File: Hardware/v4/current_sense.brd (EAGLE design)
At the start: 69.8 x 59.9 mm, 40 parts, among them J1 SCREW-TERMINAL_2_0.100, J2 SCREW-TERMINAL_2_0.100, J3 SCREW-TERMINAL_2_0.100, J4 SCREW-TERMINAL_2_0.100, U1 MAX9923H, U2 LP3985

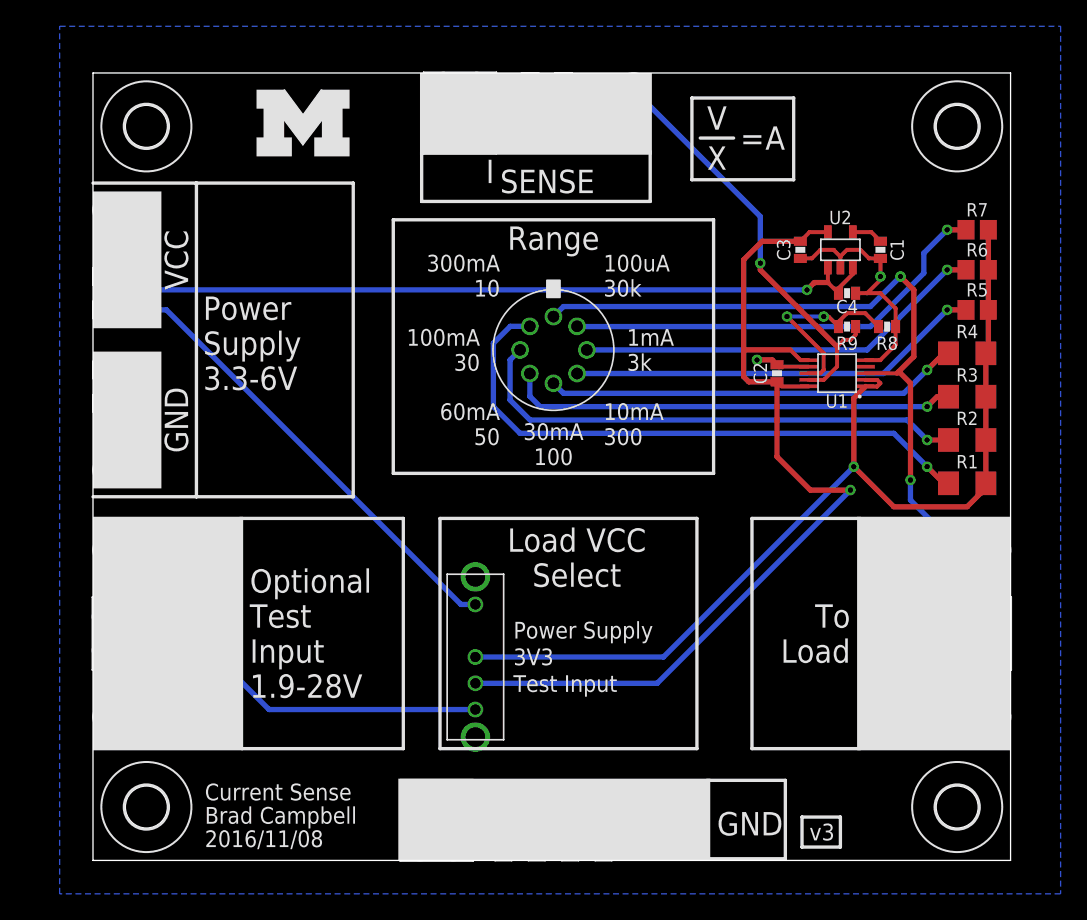
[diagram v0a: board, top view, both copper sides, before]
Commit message: Fix resistance issues, all doc on silk now
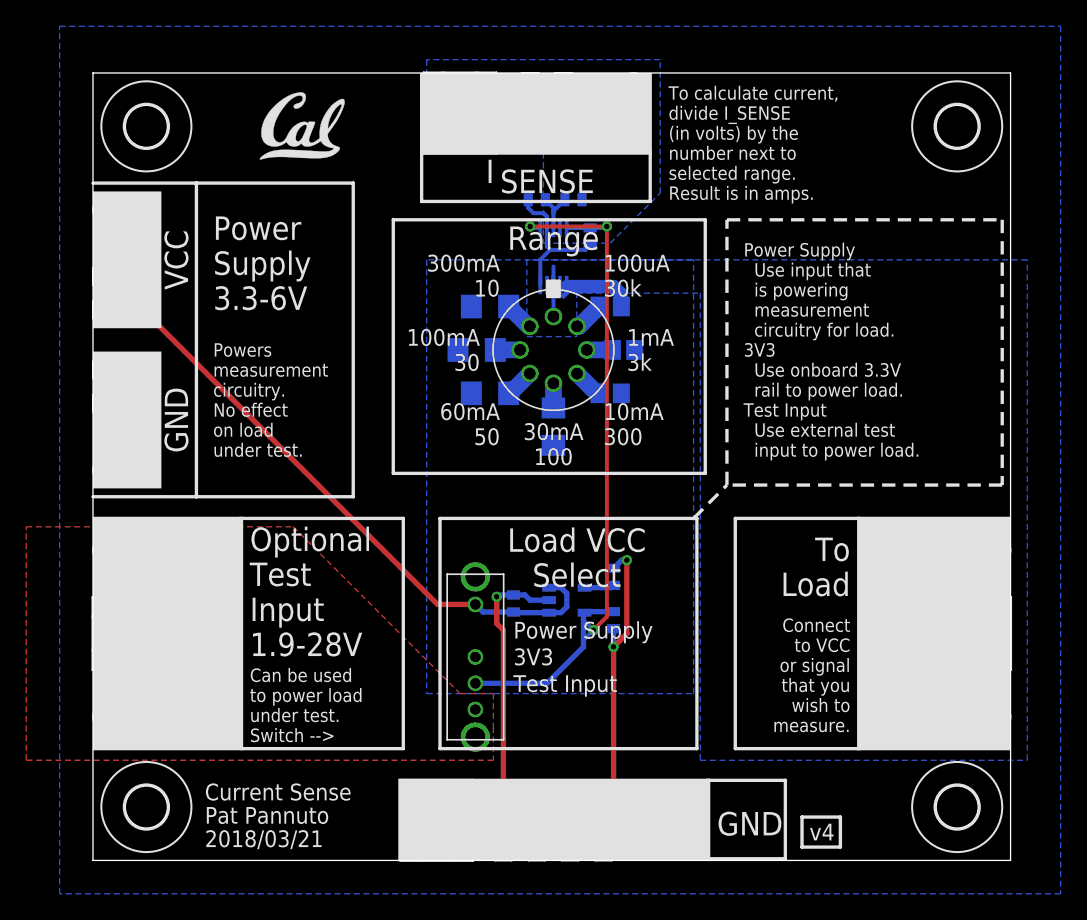
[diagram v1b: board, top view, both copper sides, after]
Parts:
- removed LOGO2: UMICH_SOLID_MEDIUM, logos:UMICH_SOLID_200MIL
- added U$1: (no value), logos:UCB_CAL_200MIL
- moved R1 38.7 mm to (30.2, 42.2), flipped to the bottom
- moved R2 38.0 mm to (29.2, 38.9), flipped to the bottom
- moved R3 36.3 mm to (30.2, 35.6), flipped to the bottom
- moved C4 34.7 mm to (32.0, 19.6), flipped to the bottom, turned to 90 degrees
- moved U2 33.8 mm to (36.1, 19.8), flipped to the bottom, turned to 90 degrees
- moved C1 32.1 mm to (39.6, 21.6), flipped to the bottom, turned to 90 degrees
- moved R4 32.0 mm to (35.1, 33.0), flipped to the bottom, turned to 270 degrees
- moved C3 31.6 mm to (39.6, 18.3), flipped to the bottom
- moved R5 28.7 mm to (39.4, 35.6), flipped to the bottom, turned to 180 degrees
- moved R7 28.5 mm to (39.4, 42.2), flipped to the bottom, turned to 180 degrees
- moved R8 28.4 mm to (33.8, 50.3), flipped to the bottom
- moved R6 27.6 mm to (40.4, 38.9), flipped to the bottom, turned to 180 degrees
- moved U1 23.3 mm to (35.1, 46.0), flipped to the bottom, turned to 0 degrees
- moved R9 23.0 mm to (36.6, 50.3), flipped to the bottom, turned to 180 degrees
- moved C2 17.6 mm to (37.8, 47.5), flipped to the bottom, turned to 270 degrees
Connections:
- net N$1 renamed RS-_100UA
- net N$2 renamed RS-_1MA
- net N$3 renamed RS-_10MA
- net N$4 renamed RS-_30MA
- net N$5 renamed RS-_60MA
- net N$6 renamed RS-_100MA
- net N$7 renamed SENSE_FB
- net N$8 renamed LDO_BYPASS
- net N$9 renamed RS-_300MA
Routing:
- net RS-: track 85.4 -> 3.81 mm, vias 2 -> 0
- net VIN: track 75.4 -> 7.31 mm, vias 1 -> 0
- net VOUT: track 52.4 -> 0.00 mm, vias 1 -> 0
- net LOAD_IN: track 50.5 -> 0.00 mm
- net POWER_SUPPLY: track 104.8 -> 59.8 mm, vias 1 -> 0
- net RS-_300MA: track 45.2 -> 2.23 mm, vias 1 -> 0
- net RS-_100MA: track 38.8 -> 1.88 mm, vias 1 -> 0
- net RS-_60MA: track 34.3 -> 2.23 mm, vias 1 -> 0
- net RS-_100UA: track 33.6 -> 2.30 mm, vias 1 -> 0
- net RS-_30MA: track 31.7 -> 1.88 mm, vias 1 -> 0
- net RS-_1MA: track 31.4 -> 1.94 mm, vias 1 -> 0
- net RS-_10MA: track 31.6 -> 2.30 mm, vias 1 -> 0
- net GND: track 37.1 -> 54.2 mm, vias 2 -> 3
- net VCC: track 73.7 -> 57.3 mm, vias 1 -> 3
- net SENSE_FB: track 14.8 -> 3.64 mm, vias 2 -> 0
- added copper zone on layer 1, net LOAD_IN
- added copper zone on layer 16, net RS-
- added copper zone on layer 16, net VIN
- added copper zone on layer 16, net VOUT
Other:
- board text added: "2018/03/21"
- board text added: "Can be used to power load under test. Switch -->"
- board text added: "Connect to VCC or signal that you wish to measure."
- board text added: "Pat Pannuto"
- board text added: "Power Supply Use input that is powering measurement circuitry for load. 3V3 Use onboard 3.3V rail to power load. Test Input Use external test input to power load."
- board text added: "Powers measurement circuitry. No effect on load under test."
- board text added: "To calculate current, divide I_SENSE (in volts) by the number next to selected range. Result is in amps."
- board text added: "v4"
- board text removed: "2016/11/08"
- board text removed: "="
- board text removed: "A"
- board text removed: "Brad Campbell"
- board text removed: "V"
- board text removed: "X"
- board text removed: "v3"

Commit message: v4: fatten more traces because why not
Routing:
- net GND: track 54.2 -> 56.3 mm, vias 3 -> 5
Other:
- board text added: "2018/03/22"
- board text removed: "2018/03/21"
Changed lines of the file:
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@@
 <setting verticaltext="up"/>
 </settings>
-<grid distance="25" unitdist="mil" unit="mil" style="lines" multiple="1" display="yes" altdistance="10" altunitdist="mil" altunit="mil"/>
+<grid distance="10" unitdist="mil" unit="mil" style="lines" multiple="1" display="yes" altdistance="10" altunitdist="mil" altunit="mil"/>
 <layers>
 <layer number="1" name="Top" color="4" fill="1" visible="yes" active="yes"/>
@@
 <text x="8.509" y="4.572" size="1.27" layer="21" font="vector" ratio="12">Current Sense</text>
 <text x="8.509" y="2.794" size="1.27" layer="21" font="vector" ratio="12">Pat Pannuto</text>
-<text x="8.509" y="1.016" size="1.27" layer="21" font="vector" ratio="12">2018/03/21</text>
+<text x="8.509" y="1.016" size="1.27" layer="21" font="vector" ratio="12">2018/03/22</text>
 <text x="55.499" y="2.159" size="1.27" layer="21" font="vector" ratio="12" align="center">v4</text>
 <wire x1="53.975" y1="1.016" x2="56.896" y2="1.016" width="0.254" layer="21"/>
@@
 <vertex x="-2.54" y="-2.54"/>
 </polygon>
-<wire x1="38.862" y1="3.81" x2="39.624" y2="4.572" width="0.4064" layer="1"/>
-<wire x1="39.624" y1="4.572" x2="39.624" y2="16.256" width="0.4064" layer="1"/>
+<wire x1="38.862" y1="3.81" x2="39.624" y2="4.572" width="0.8128" layer="1"/>
+<wire x1="39.624" y1="4.572" x2="39.624" y2="16.256" width="0.8128" layer="1"/>
 <via x="39.624" y="16.256" extent="1-16" drill="0.4064"/>
 <wire x1="39.624" y1="16.256" x2="39.624" y2="17.638" width="0.4064" layer="16"/>
-<wire x1="39.624" y1="16.256" x2="40.64" y2="17.272" width="0.4064" layer="1"/>
-<wire x1="40.64" y1="17.272" x2="40.64" y2="22.86" width="0.4064" layer="1"/>
+<wire x1="39.624" y1="16.256" x2="40.64" y2="17.272" width="0.8128" layer="1"/>
+<wire x1="40.64" y1="17.272" x2="40.64" y2="22.86" width="0.8128" layer="1"/>
 <via x="40.64" y="22.86" extent="1-16" drill="0.4064"/>
-<wire x1="39.624" y1="22.24" x2="40.244" y2="22.86" width="0.4064" layer="16"/>
-<wire x1="40.244" y1="22.86" x2="40.64" y2="22.86" width="0.4064" layer="16"/>
+<wire x1="39.624" y1="22.24" x2="40.244" y2="22.86" width="0.8128" layer="16"/>
+<wire x1="40.244" y1="22.86" x2="40.64" y2="22.86" width="0.8128" layer="16"/>
 <wire x1="32.004" y1="20.208" x2="32.878" y2="20.208" width="0.4064" layer="16"/>
 <wire x1="32.878" y1="20.208" x2="33.274" y2="19.812" width="0.4064" layer="16"/>
@@
 <wire x1="30.876" y1="20.208" x2="30.734" y2="20.066" width="0.4064" layer="16"/>
 <via x="30.734" y="20.066" extent="1-16" drill="0.4064"/>
-<wire x1="30.734" y1="20.066" x2="30.734" y2="18.034" width="0.4064" layer="1"/>
-<wire x1="30.734" y1="18.034" x2="31.242" y2="17.526" width="0.4064" layer="1"/>
-<wire x1="31.242" y1="17.526" x2="31.242" y2="3.81" width="0.4064" layer="1"/>
+<wire x1="30.734" y1="20.066" x2="30.734" y2="18.034" width="0.8128" layer="1"/>
+<wire x1="30.734" y1="18.034" x2="31.242" y2="17.526" width="0.8128" layer="1"/>
+<wire x1="31.242" y1="17.526" x2="31.242" y2="3.81" width="0.8128" layer="1"/>
 <wire x1="33.132" y1="50.292" x2="33.132" y2="49.672" width="0.3048" layer="16"/>
 <wire x1="33.132" y1="49.672" x2="33.528" y2="49.276" width="0.3048" layer="16"/>
@@
 <wire x1="34.552" y1="49.014" x2="34.552" y2="48.144" width="0.3048" layer="16"/>
 <wire x1="34.29" y1="49.276" x2="34.552" y2="49.014" width="0.3048" layer="16"/>
-<wire x1="34.552" y1="48.144" x2="34.552" y2="46.728" width="0.3048" layer="16"/>
-<wire x1="34.552" y1="46.728" x2="34.798" y2="46.482" width="0.3048" layer="16"/>
-<wire x1="34.798" y1="46.482" x2="37.48" y2="46.482" width="0.3048" layer="16"/>
-<wire x1="37.48" y1="46.482" x2="37.846" y2="46.848" width="0.3048" layer="16"/>
-<wire x1="34.052" y1="43.804" x2="34.052" y2="45.736" width="0.3048" layer="16"/>
-<wire x1="34.052" y1="45.736" x2="34.798" y2="46.482" width="0.3048" layer="16"/>
+<via x="33.274" y="44.958" extent="1-16" drill="0.4064"/>
+<wire x1="37.846" y1="46.848" x2="34.686" y2="46.848" width="0.3048" layer="16"/>
+<wire x1="34.544" y1="46.99" x2="34.686" y2="46.848" width="0.3048" layer="16"/>
+<wire x1="34.552" y1="48.144" x2="34.544" y2="48.136" width="0.3048" layer="16"/>
+<wire x1="34.544" y1="48.136" x2="34.544" y2="46.99" width="0.3048" layer="16"/>
+<wire x1="33.274" y1="44.958" x2="30.988" y2="47.244" width="0.3048" layer="1"/>
+<wire x1="30.988" y1="47.244" x2="30.226" y2="47.244" width="0.3048" layer="1"/>
+<via x="30.226" y="47.244" extent="1-16" drill="0.4064"/>
+<wire x1="34.052" y1="43.804" x2="34.052" y2="44.18" width="0.3048" layer="16"/>
+<wire x1="34.052" y1="44.18" x2="33.274" y2="44.958" width="0.3048" layer="16"/>
 </signal>
 <signal name="VCC">
@@
 <wire x1="39.624" y1="18.938" x2="37.494" y2="18.938" width="0.4064" layer="16"/>
 <wire x1="37.494" y1="18.938" x2="37.418" y2="18.862" width="0.4064" layer="16"/>
-<wire x1="29.11" y1="13.486" x2="34.568" y2="13.486" width="0.4064" layer="16"/>
-<wire x1="37.338" y1="16.256" x2="34.568" y2="13.486" width="0.4064" layer="16"/>
+<wire x1="29.11" y1="13.486" x2="34.568" y2="13.486" width="0.8128" layer="16"/>
+<wire x1="37.338" y1="16.256" x2="34.568" y2="13.486" width="0.8128" layer="16"/>
 <wire x1="37.418" y1="18.862" x2="37.338" y2="18.782" width="0.4064" layer="16"/>
-<wire x1="37.338" y1="18.782" x2="37.338" y2="18.288" width="0.4064" layer="16"/>
-<wire x1="37.338" y1="18.288" x2="37.338" y2="16.764" width="0.4064" layer="16"/>
-<wire x1="37.338" y1="16.764" x2="37.338" y2="16.256" width="0.4064" layer="16"/>
+<wire x1="37.338" y1="18.782" x2="37.338" y2="18.288" width="0.8128" layer="16"/>
+<wire x1="37.338" y1="18.288" x2="37.338" y2="16.764" width="0.8128" layer="16"/>
+<wire x1="37.338" y1="16.764" x2="37.338" y2="16.256" width="0.8128" layer="16"/>
 <wire x1="36.052" y1="48.144" x2="37.842" y2="48.144" width="0.3048" layer="16"/>
 <wire x1="37.842" y1="48.144" x2="37.846" y2="48.148" width="0.3048" layer="16"/>
@@
 <wire x1="33.39" y1="48.144" x2="33.274" y2="48.26" width="0.3048" layer="16"/>
 <via x="33.274" y="48.26" extent="1-16" drill="0.4064"/>
-<wire x1="33.274" y1="48.26" x2="39.116" y2="48.26" width="0.3048" layer="1"/>
+<wire x1="33.274" y1="48.26" x2="39.116" y2="48.26" width="0.8128" layer="1"/>
 <via x="39.116" y="48.26" extent="1-16" drill="0.4064"/>
 <wire x1="37.846" y1="48.148" x2="39.004" y2="48.148" width="0.3048" layer="16"/>
 <wire x1="39.004" y1="48.148" x2="39.116" y2="48.26" width="0.3048" layer="16"/>
-<wire x1="39.116" y1="48.26" x2="39.116" y2="18.542" width="0.3048" layer="1"/>
-<wire x1="39.116" y1="18.542" x2="38.1" y2="17.526" width="0.3048" layer="1"/>
+<wire x1="39.116" y1="48.26" x2="39.116" y2="18.542" width="0.8128" layer="1"/>
+<wire x1="39.116" y1="18.542" x2="38.1" y2="17.526" width="0.8128" layer="1"/>
 <via x="38.1" y="17.526" extent="1-16" drill="0.4064"/>
-<wire x1="38.1" y1="17.526" x2="37.338" y2="18.288" width="0.3048" layer="16"/>
-<wire x1="38.1" y1="17.526" x2="37.338" y2="16.764" width="0.3048" layer="16"/>
+<wire x1="38.1" y1="17.526" x2="37.338" y2="18.288" width="0.8128" layer="16"/>
+<wire x1="38.1" y1="17.526" x2="37.338" y2="16.764" width="0.8128" layer="16"/>
 </signal>
 <signal name="RS-">
@@
 <contactref element="S1" pad="C"/>
 <polygon width="0.2032" layer="16" isolate="0.3048" thermals="no">
-<vertex x="33.02" y="45.72"/>
-<vertex x="33.02" y="39.878"/>
+<vertex x="31.496" y="46.736"/>
+<vertex x="31.496" y="39.878"/>
 <vertex x="36.83" y="39.878"/>
 <vertex x="36.83" y="43.18"/>
@@
 <vertex x="46.228" y="7.62"/>
 <vertex x="71.12" y="7.62"/>
-<vertex x="71.12" y="45.72"/>
+<vertex x="71.12" y="46.736"/>
 </polygon>
 <wire x1="35.052" y1="43.804" x2="35.052" y2="41.402" width="0.3048" layer="16"/>
@@
 <contactref element="TP3" pad="TESTPOINT"/>
 <contactref element="S2" pad="1"/>
-<wire x1="1.27" y1="44.45" x2="3.81" y2="44.45" width="0.4064" layer="1"/>
-<wire x1="1.27" y1="49.53" x2="1.27" y2="44.45" width="0.4064" layer="1"/>
-<wire x1="1.27" y1="41.91" x2="3.81" y2="41.91" width="0.4064" layer="1"/>
-<wire x1="1.27" y1="41.91" x2="1.27" y2="44.45" width="0.4064" layer="1"/>
-<wire x1="3.81" y1="41.91" x2="3.81" y2="44.45" width="0.4064" layer="1"/>
-<wire x1="3.81" y1="41.91" x2="26.234" y2="19.486" width="0.4064" layer="1"/>
-<wire x1="26.234" y1="19.486" x2="29.11" y2="19.486" width="0.4064" layer="1"/>
-<wire x1="29.11" y1="19.486" x2="29.688" y2="18.908" width="0.4064" layer="16"/>
-<wire x1="29.688" y1="18.908" x2="32.004" y2="18.908" width="0.4064" layer="16"/>
+<wire x1="1.27" y1="44.45" x2="3.81" y2="44.45" width="0.8128" layer="1"/>
+<wire x1="1.27" y1="49.53" x2="1.27" y2="44.45" width="0.8128" layer="1"/>
+<wire x1="1.27" y1="41.91" x2="3.81" y2="41.91" width="0.8128" layer="1"/>
+<wire x1="1.27" y1="41.91" x2="1.27" y2="44.45" width="0.8128" layer="1"/>
+<wire x1="3.81" y1="41.91" x2="3.81" y2="44.45" width="0.8128" layer="1"/>
+<wire x1="3.81" y1="41.91" x2="26.234" y2="19.486" width="0.8128" layer="1"/>
+<wire x1="26.234" y1="19.486" x2="29.11" y2="19.486" width="0.8128" layer="1"/>
+<wire x1="29.11" y1="19.486" x2="29.688" y2="18.908" width="0.8128" layer="16"/>
+<wire x1="29.688" y1="18.908" x2="32.004" y2="18.908" width="0.8128" layer="16"/>
 <wire x1="32.004" y1="18.908" x2="32.05" y2="18.862" width="0.4064" layer="16"/>
-<wire x1="32.05" y1="18.862" x2="34.718" y2="18.862" width="0.4064" layer="16"/>
+<wire x1="32.05" y1="18.862" x2="34.718" y2="18.862" width="0.8128" layer="16"/>
 <wire x1="34.718" y1="20.762" x2="35.626" y2="20.762" width="0.4064" layer="16"/>
 <wire x1="35.626" y1="20.762" x2="36.068" y2="20.32" width="0.4064" layer="16"/>
